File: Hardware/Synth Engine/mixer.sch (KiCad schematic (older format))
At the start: 62 parts, among them J2 Audio-Jack-2_Switch, U3 TL074, U8 PT2399

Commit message: add delay connector to main board and route it.
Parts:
- removed RV13: 20kA, Potentiometers:Potentiometer_Bourns_PTV09A-1_Horizontal, symbol POT
- removed RV14: 20k, Potentiometers:Potentiometer_Bourns_PTV09A-1_Horizontal, symbol POT
- removed RV15, RV16: 50kA, Potentiometers:Potentiometer_Bourns_PTV09A-1_Horizontal, symbol POT
- added J12: Conn_01x06, Pin_Headers:Pin_Header_Straight_1x06_Pitch2.54mm, symbol Conn_01x06
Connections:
- net labels added: delay_fb_ctrl_in, delay_fb_ctrl_out, delay_time_in, delay_time_out
- wire segments 140 -> 132
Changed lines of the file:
@@
 	0    1    1    0
-$EndComp
-$Comp
-L POT RV13
-U 1 1 5C54BC7D
-P 3650 2800
-F 0 "RV13" V 3475 2800 50  0000 C CNN
-F 1 "20kA" V 3550 2800 50  0000 C CNN
-F 2 "Potentiometers:Potentiometer_Bourns_PTV09A-1_Horizontal" H 3650 2800 50  0001 C CNN
-F 3 "" H 3650 2800 50  0001 C CNN
-	1    3650 2800
-	0    1    1    0
-$EndComp
-$Comp
-L GND #PWR072
-U 1 1 5C54BEBB
-P 3300 2850
-F 0 "#PWR072" H 3300 2600 50  0001 C CNN
-F 1 "GND" H 3300 2700 50  0000 C CNN
-F 2 "" H 3300 2850 50  0001 C CNN
-F 3 "" H 3300 2850 50  0001 C CNN
-	1    3300 2850
-	1    0    0    -1
 $EndComp
 Text Notes 2400 3050 0    60   ~ 0
@@
 $EndComp
 $Comp
-L GND #PWR073
+L GND #PWR072
 U 1 1 5C54C375
 P 4000 3250
-F 0 "#PWR073" H 4000 3000 50  0001 C CNN
+F 0 "#PWR072" H 4000 3000 50  0001 C CNN
 F 1 "GND" H 4000 3100 50  0000 C CNN
 F 2 "" H 4000 3250 50  0001 C CNN
@@
 $EndComp
 $Comp
-L GND #PWR074
+L GND #PWR073
 U 1 1 5C54C409
 P 4250 3400
-F 0 "#PWR074" H 4250 3150 50  0001 C CNN
+F 0 "#PWR073" H 4250 3150 50  0001 C CNN
 F 1 "GND" H 4250 3250 50  0000 C CNN
 F 2 "" H 4250 3400 50  0001 C CNN
@@
 $EndComp
 $Comp
-L GND #PWR075
+L GND #PWR074
 U 1 1 5C54D840
 P 6400 2650
-F 0 "#PWR075" H 6400 2400 50  0001 C CNN
+F 0 "#PWR074" H 6400 2400 50  0001 C CNN
 F 1 "GND" H 6400 2500 50  0000 C CNN
 F 2 "" H 6400 2650 50  0001 C CNN
@@
 $EndComp
 $Comp
-L GND #PWR076
+L GND #PWR075
 U 1 1 5C54DB09
 P 6850 2500
-F 0 "#PWR076" H 6850 2250 50  0001 C CNN
+F 0 "#PWR075" H 6850 2250 50  0001 C CNN
 F 1 "GND" H 6850 2350 50  0000 C CNN
 F 2 "" H 6850 2500 50  0001 C CNN
@@
 $EndComp
 $Comp
-L POT RV15
-U 1 1 5C54DE3E
-P 7400 2450
-F 0 "RV15" V 7225 2450 50  0000 C CNN
-F 1 "50kA" V 7300 2450 50  0000 C CNN
-F 2 "Potentiometers:Potentiometer_Bourns_PTV09A-1_Horizontal" H 7400 2450 50  0001 C CNN
-F 3 "" H 7400 2450 50  0001 C CNN
-	1    7400 2450
-	1    0    0    -1
-$EndComp
-$Comp
-L GND #PWR077
-U 1 1 5C54DF89
-P 7400 2600
-F 0 "#PWR077" H 7400 2350 50  0001 C CNN
-F 1 "GND" H 7400 2450 50  0000 C CNN
-F 2 "" H 7400 2600 50  0001 C CNN
-F 3 "" H 7400 2600 50  0001 C CNN
-	1    7400 2600
-	1    0    0    -1
-$EndComp
-$Comp
 L R R73
 U 1 1 5C54E024
@@
 	4200 2800 4350 2800
 Wire Wire Line
-	3300 2850 3300 2800
-Wire Wire Line
-	3300 2800 3500 2800
-Wire Wire Line
 	3650 2950 3850 2950
-Wire Wire Line
-	3850 2950 3850 2800
-Connection ~ 3850 2800
 Wire Wire Line
 	4250 3200 4250 3100
@@
 Connection ~ 6850 2250
 Wire Wire Line
-	7400 2300 7400 2250
-Wire Wire Line
-	7400 2250 7250 2250
+	7250 2250 7400 2250
 Wire Wire Line
 	5350 2200 5700 2200
@@
 $EndComp
 $Comp
-L GND #PWR078
+L GND #PWR076
 U 1 1 5C54F6A3
 P 5600 1450
-F 0 "#PWR078" H 5600 1200 50  0001 C CNN
+F 0 "#PWR076" H 5600 1200 50  0001 C CNN
 F 1 "GND" H 5600 1300 50  0000 C CNN
 F 2 "" H 5600 1450 50  0001 C CNN
@@
 $EndComp
 $Comp
-L GND #PWR079
+L GND #PWR077
 U 1 1 5C54FA05
 P 7150 1800
-F 0 "#PWR079" H 7150 1550 50  0001 C CNN
+F 0 "#PWR077" H 7150 1550 50  0001 C CNN
 F 1 "GND" H 7150 1650 50  0000 C CNN
 F 2 "" H 7150 1800 50  0001 C CNN
@@
 Text Label 4450 4400 0    60   ~ 0
 delay_in
-Text Label 9400 2350 0    60   ~ 0
+Text Label 9250 2100 0    60   ~ 0
 delay_out
 Wire Wire Line
-	9150 2100 9000 2100
+	9000 2100 9250 2100
 $Comp
 L R R74
@@
 $EndComp
 $Comp
-L GND #PWR080
+L GND #PWR078
 U 1 1 5C55157C
 P 8900 4800
-F 0 "#PWR080" H 8900 4550 50  0001 C CNN
+F 0 "#PWR078" H 8900 4550 50  0001 C CNN
 F 1 "GND" H 8900 4650 50  0000 C CNN
 F 2 "" H 8900 4800 50  0001 C CNN
@@
 $EndComp
 $Comp
-L +15V #PWR081
+L +15V #PWR079
 U 1 1 5C551582
 P 8900 4200
-F 0 "#PWR081" H 8900 4050 50  0001 C CNN
+F 0 "#PWR079" H 8900 4050 50  0001 C CNN
 F 1 "+15V" H 8900 4340 50  0000 C CNN
 F 2 "" H 8900 4200 50  0001 C CNN
@@
 	8450 4750 8450 4600
 $Comp
-L POT RV16
-U 1 1 5C5521F6
-P 9150 2350
-F 0 "RV16" V 8975 2350 50  0000 C CNN
-F 1 "50kA" V 9050 2350 50  0000 C CNN
-F 2 "Potentiometers:Potentiometer_Bourns_PTV09A-1_Horizontal" H 9150 2350 50  0001 C CNN
-F 3 "" H 9150 2350 50  0001 C CNN
-	1    9150 2350
-	1    0    0    -1
-$EndComp
-Wire Wire Line
-	9400 2350 9300 2350
-Wire Wire Line
-	9150 2200 9150 2100
-$Comp
-L GND #PWR082
-U 1 1 5C552581
-P 9150 2500
-F 0 "#PWR082" H 9150 2250 50  0001 C CNN
-F 1 "GND" H 9150 2350 50  0000 C CNN
-F 2 "" H 9150 2500 50  0001 C CNN
-F 3 "" H 9150 2500 50  0001 C CNN
-	1    9150 2500
-	1    0    0    -1
-$EndComp
-$Comp
 L R R59
 U 1 1 5C5902E2
@@
 $EndComp
 $Comp
-L GND #PWR083
+L GND #PWR080
 U 1 1 5C5902F7
 P 6400 4150
-F 0 "#PWR083" H 6400 3900 50  0001 C CNN
+F 0 "#PWR080" H 6400 3900 50  0001 C CNN
 F 1 "GND" H 6400 4000 50  0000 C CNN
 F 2 "" H 6400 4150 50  0001 C CNN
@@
 $EndComp
 $Comp
-L +15V #PWR084
+L +15V #PWR081
 U 1 1 5C5902FD
 P 6400 3550
-F 0 "#PWR084" H 6400 3400 50  0001 C CNN
+F 0 "#PWR081" H 6400 3400 50  0001 C CNN
 F 1 "+15V" H 6400 3690 50  0000 C CNN
 F 2 "" H 6400 3550 50  0001 C CNN
@@
 $EndComp
 $Comp
-L GND #PWR085
+L GND #PWR082
 U 1 1 5C59059B
 P 6400 5700
-F 0 "#PWR085" H 6400 5450 50  0001 C CNN
+F 0 "#PWR082" H 6400 5450 50  0001 C CNN
 F 1 "GND" H 6400 5550 50  0000 C CNN
 F 2 "" H 6400 5700 50  0001 C CNN
@@
 $EndComp
 $Comp
-L +15V #PWR086
+L +15V #PWR083
 U 1 1 5C5905A1
 P 6400 5100
-F 0 "#PWR086" H 6400 4950 50  0001 C CNN
+F 0 "#PWR083" H 6400 4950 50  0001 C CNN
 F 1 "+15V" H 6400 5240 50  0000 C CNN
 F 2 "" H 6400 5100 50  0001 C CNN
@@
 Text Label 4900 5500 0    60   ~ 0
 delay_out
-$Comp
-L POT RV14
-U 1 1 5C5914EB
-P 5150 4700
-F 0 "RV14" V 4975 4700 50  0000 C CNN
-F 1 "20k" V 5050 4700 50  0000 C CNN
-F 2 "Potentiometers:Potentiometer_Bourns_PTV09A-1_Horizontal" H 5150 4700 50  0001 C CNN
-F 3 "" H 5150 4700 50  0001 C CNN
-	1    5150 4700
-	1    0    0    -1
-$EndComp
 Wire Wire Line
 	5150 4550 5150 3950
@@
 	5150 4850 5150 5500
 Connection ~ 5150 5500
-$Comp
-L GND #PWR087
-U 1 1 5C5917F8
-P 5400 4750
-F 0 "#PWR087" H 5400 4500 50  0001 C CNN
-F 1 "GND" H 5400 4600 50  0000 C CNN
-F 2 "" H 5400 4750 50  0001 C CNN
-F 3 "" H 5400 4750 50  0001 C CNN
-	1    5400 4750
-	1    0    0    -1
-$EndComp
-Wire Wire Line
-	5400 4750 5400 4700
-Wire Wire Line
-	5400 4700 5300 4700
 Wire Wire Line
 	7350 3850 7350 4600
 Wire Wire Line
 	7350 5400 7350 4750
+$Comp
+L Conn_01x06 J12
+U 1 1 5C651FB4
+P 9550 2900
+F 0 "J12" H 9550 3200 50  0000 C CNN
+F 1 "Conn_01x06" H 9550 2500 50  0000 C CNN
+F 2 "Pin_Headers:Pin_Header_Straight_1x06_Pitch2.54mm" H 9550 2900 50  0001 C CNN
+F 3 "" H 9550 2900 50  0001 C CNN
+	1    9550 2900
+	1    0    0    -1
+$EndComp
+Text Label 7400 2250 0    60   ~ 0
+delay_fb_ctrl_in
+Text Label 7550 2450 2    60   ~ 0
+delay_fb_ctrl_out
+Text Label 9350 2700 2    60   ~ 0
+delay_fb_ctrl_in
+Text Label 9350 2800 2    60   ~ 0
+delay_fb_ctrl_out
+Text Label 3800 2800 2    60   ~ 0
+delay_time_in
+Text Label 3650 2950 2    60   ~ 0
+delay_time_out
+Text Label 9350 2900 2    60   ~ 0
+delay_time_in
+Text Label 9350 3000 2    60   ~ 0
+delay_time_out
+Text Label 9350 3100 2    60   ~ 0
+delay_in
+Text Label 9350 3200 2    60   ~ 0
+delay_out
+$Comp
+L GND #PWR084
+U 1 1 5C652A53
+P 3850 2950
+F 0 "#PWR084" H 3850 2700 50  0001 C CNN
+F 1 "GND" H 3850 2800 50  0000 C CNN
+F 2 "" H 3850 2950 50  0001 C CNN
+F 3 "" H 3850 2950 50  0001 C CNN
+	1    3850 2950
+	1    0    0    -1
+$EndComp
 $EndSCHEMATC

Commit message: fix remaining connector placement. Routing still WIP
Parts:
- removed J12: Conn_01x06, Pin_Headers:Pin_Header_Straight_1x06_Pitch2.54mm, symbol Conn_01x06
- added J5: Conn_01x08, Pin_Headers:Pin_Header_Straight_1x08_Pitch2.54mm, symbol Conn_01x08
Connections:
- net labels added: lfo_freq_in, lfo_freq_out
- wire segments 132 -> 134
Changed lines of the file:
@@
 Wire Wire Line
 	7350 5400 7350 4750
-$Comp
-L Conn_01x06 J12
-U 1 1 5C651FB4
-P 9550 2900
-F 0 "J12" H 9550 3200 50  0000 C CNN
-F 1 "Conn_01x06" H 9550 2500 50  0000 C CNN
-F 2 "Pin_Headers:Pin_Header_Straight_1x06_Pitch2.54mm" H 9550 2900 50  0001 C CNN
-F 3 "" H 9550 2900 50  0001 C CNN
-	1    9550 2900
-	1    0    0    -1
-$EndComp
 Text Label 7400 2250 0    60   ~ 0
 delay_fb_ctrl_in
@@
 	1    0    0    -1
 $EndComp
+Wire Wire Line
+	9000 3300 9350 3300
+Wire Wire Line
+	9000 3400 9350 3400
+Text HLabel 9000 3300 0    60   Output ~ 0
+lfo_freq_in
+Text HLabel 9000 3400 0    60   Input ~ 0
+lfo_freq_out
+$Comp
+L Conn_01x08 J5
+U 1 1 5C702327
+P 9550 3000
+F 0 "J5" H 9550 3400 50  0000 C CNN
+F 1 "Conn_01x08" H 9550 2500 50  0000 C CNN
+F 2 "Pin_Headers:Pin_Header_Straight_1x08_Pitch2.54mm" H 9550 3000 50  0001 C CNN
+F 3 "" H 9550 3000 50  0001 C CNN
+	1    9550 3000
+	1    0    0    -1
+$EndComp

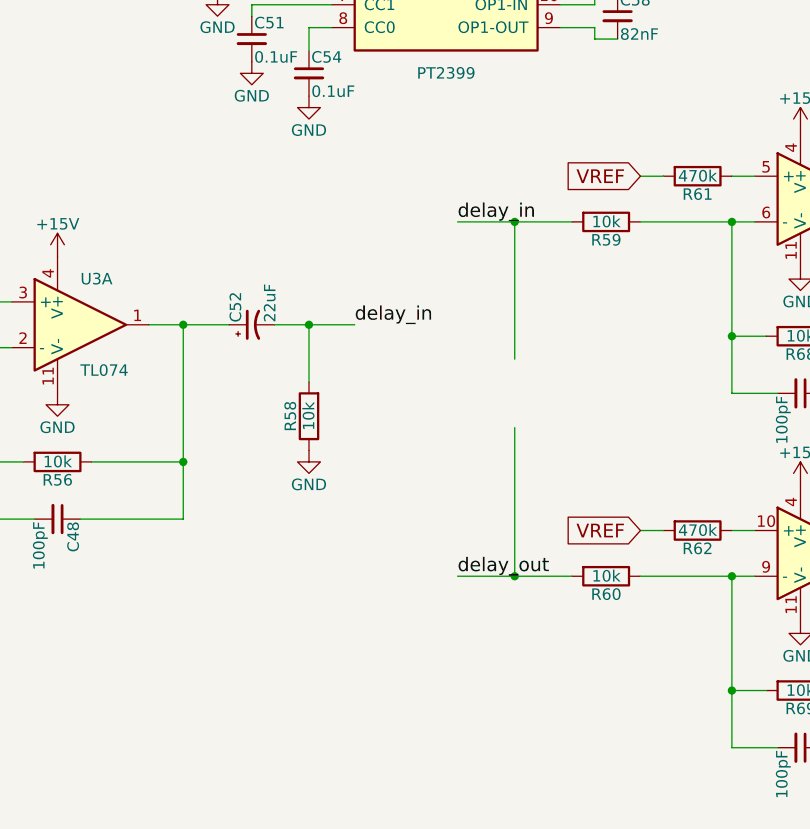
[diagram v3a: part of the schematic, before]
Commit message: redo connector routing with 2-row connectors
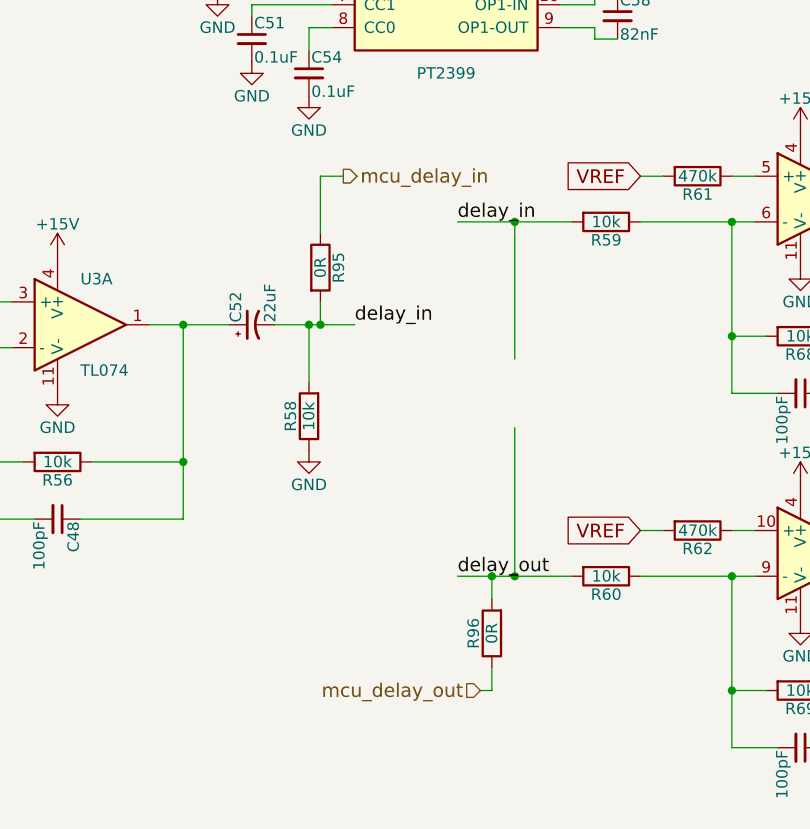
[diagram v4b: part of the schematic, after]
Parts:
- added R95, R96: 0R, digikey-footprints:0805, symbol R
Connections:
- net delay_in: now also R95.2
- net delay_out: now also R96.2
- new net mcu_delay_in: R95.1
- new net mcu_delay_out: R96.1
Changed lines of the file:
@@
 $EndComp
 $Comp
-L GND #PWR061
+L GND #PWR84
 U 1 1 5C394C8E
 P 10800 4700
-F 0 "#PWR061" H 10800 4450 50  0001 C CNN
+F 0 "#PWR84" H 10800 4450 50  0001 C CNN
 F 1 "GND" H 10800 4550 50  0000 C CNN
 F 2 "" H 10800 4700 50  0001 C CNN
@@
 $EndComp
 $Comp
-L GND #PWR062
+L GND #PWR62
 U 1 1 5C396479
 P 3150 4700
-F 0 "#PWR062" H 3150 4450 50  0001 C CNN
+F 0 "#PWR62" H 3150 4450 50  0001 C CNN
 F 1 "GND" H 3150 4550 50  0000 C CNN
 F 2 "" H 3150 4700 50  0001 C CNN
@@
 $EndComp
 $Comp
-L GND #PWR063
+L GND #PWR83
 U 1 1 5C39665C
 P 10200 5050
-F 0 "#PWR063" H 10200 4800 50  0001 C CNN
+F 0 "#PWR83" H 10200 4800 50  0001 C CNN
 F 1 "GND" H 10200 4900 50  0000 C CNN
 F 2 "" H 10200 5050 50  0001 C CNN
@@
 $EndComp
 $Comp
-L +15V #PWR064
+L +15V #PWR61
 U 1 1 5C396690
 P 3150 4100
-F 0 "#PWR064" H 3150 3950 50  0001 C CNN
+F 0 "#PWR61" H 3150 3950 50  0001 C CNN
 F 1 "+15V" H 3150 4240 50  0000 C CNN
 F 2 "" H 3150 4100 50  0001 C CNN
@@
 $EndComp
 $Comp
-L GND #PWR065
+L GND #PWR70
 U 1 1 5C55ADAC
 P 4250 4950
-F 0 "#PWR065" H 4250 4700 50  0001 C CNN
+F 0 "#PWR70" H 4250 4700 50  0001 C CNN
 F 1 "GND" H 4250 4800 50  0000 C CNN
 F 2 "" H 4250 4950 50  0001 C CNN
@@
 $EndComp
 $Comp
-L +5V #PWR066
+L +5V #PWR68
 U 1 1 5C54B4C5
 P 4100 1900
-F 0 "#PWR066" H 4100 1750 50  0001 C CNN
+F 0 "#PWR68" H 4100 1750 50  0001 C CNN
 F 1 "+5V" H 4100 2040 50  0000 C CNN
 F 2 "" H 4100 1900 50  0001 C CNN
@@
 $EndComp
 $Comp
-L GND #PWR067
+L GND #PWR63
 U 1 1 5C54B862
 P 3250 2350
-F 0 "#PWR067" H 3250 2100 50  0001 C CNN
+F 0 "#PWR63" H 3250 2100 50  0001 C CNN
 F 1 "GND" H 3250 2200 50  0000 C CNN
 F 2 "" H 3250 2350 50  0001 C CNN
@@
 $EndComp
 $Comp
-L GND #PWR068
+L GND #PWR64
 U 1 1 5C54B8B0
 P 3600 2350
-F 0 "#PWR068" H 3600 2100 50  0001 C CNN
+F 0 "#PWR64" H 3600 2100 50  0001 C CNN
 F 1 "GND" H 3600 2200 50  0000 C CNN
 F 2 "" H 3600 2350 50  0001 C CNN
@@
 $EndComp
 $Comp
-L GND #PWR069
+L GND #PWR71
 U 1 1 5C54B8F7
 P 4350 2400
-F 0 "#PWR069" H 4350 2150 50  0001 C CNN
+F 0 "#PWR71" H 4350 2150 50  0001 C CNN
 F 1 "GND" H 4350 2250 50  0000 C CNN
 F 2 "" H 4350 2400 50  0001 C CNN
@@
 $EndComp
 $Comp
-L GND #PWR070
+L GND #PWR67
 U 1 1 5C54B9BF
 P 4050 2450
-F 0 "#PWR070" H 4050 2200 50  0001 C CNN
+F 0 "#PWR67" H 4050 2200 50  0001 C CNN
 F 1 "GND" H 4050 2300 50  0000 C CNN
 F 2 "" H 4050 2450 50  0001 C CNN
@@
 $EndComp
 $Comp
-L GND #PWR071
+L GND #PWR72
 U 1 1 5C54BB6A
 P 4350 2500
-F 0 "#PWR071" H 4350 2250 50  0001 C CNN
+F 0 "#PWR72" H 4350 2250 50  0001 C CNN
 F 1 "GND" H 4350 2350 50  0000 C CNN
 F 2 "" H 4350 2500 50  0001 C CNN
@@
 $EndComp
 $Comp
-L GND #PWR072
+L GND #PWR66
 U 1 1 5C54C375
 P 4000 3250
-F 0 "#PWR072" H 4000 3000 50  0001 C CNN
+F 0 "#PWR66" H 4000 3000 50  0001 C CNN
 F 1 "GND" H 4000 3100 50  0000 C CNN
 F 2 "" H 4000 3250 50  0001 C CNN
@@
 $EndComp
 $Comp
-L GND #PWR073
+L GND #PWR69
 U 1 1 5C54C409
 P 4250 3400
-F 0 "#PWR073" H 4250 3150 50  0001 C CNN
+F 0 "#PWR69" H 4250 3150 50  0001 C CNN
 F 1 "GND" H 4250 3250 50  0000 C CNN
 F 2 "" H 4250 3400 50  0001 C CNN
@@
 $EndComp
 $Comp
-L GND #PWR074
+L GND #PWR74
 U 1 1 5C54D840
 P 6400 2650
-F 0 "#PWR074" H 6400 2400 50  0001 C CNN
+F 0 "#PWR74" H 6400 2400 50  0001 C CNN
 F 1 "GND" H 6400 2500 50  0000 C CNN
 F 2 "" H 6400 2650 50  0001 C CNN
@@
 $EndComp
 $Comp
-L GND #PWR075
+L GND #PWR79
 U 1 1 5C54DB09
 P 6850 2500
-F 0 "#PWR075" H 6850 2250 50  0001 C CNN
+F 0 "#PWR79" H 6850 2250 50  0001 C CNN
 F 1 "GND" H 6850 2350 50  0000 C CNN
 F 2 "" H 6850 2500 50  0001 C CNN
@@
 $EndComp
 $Comp
-L GND #PWR076
+L GND #PWR73
 U 1 1 5C54F6A3
 P 5600 1450
-F 0 "#PWR076" H 5600 1200 50  0001 C CNN
+F 0 "#PWR73" H 5600 1200 50  0001 C CNN
 F 1 "GND" H 5600 1300 50  0000 C CNN
 F 2 "" H 5600 1450 50  0001 C CNN
@@
 $EndComp
 $Comp
-L GND #PWR077
+L GND #PWR80
 U 1 1 5C54FA05
 P 7150 1800
-F 0 "#PWR077" H 7150 1550 50  0001 C CNN
+F 0 "#PWR80" H 7150 1550 50  0001 C CNN
 F 1 "GND" H 7150 1650 50  0000 C CNN
 F 2 "" H 7150 1800 50  0001 C CNN
@@
 $EndComp
 $Comp
-L GND #PWR078
+L GND #PWR82
 U 1 1 5C55157C
 P 8900 4800
-F 0 "#PWR078" H 8900 4550 50  0001 C CNN
+F 0 "#PWR82" H 8900 4550 50  0001 C CNN
 F 1 "GND" H 8900 4650 50  0000 C CNN
 F 2 "" H 8900 4800 50  0001 C CNN
@@
 $EndComp
 $Comp
-L +15V #PWR079
+L +15V #PWR81
 U 1 1 5C551582
 P 8900 4200
-F 0 "#PWR079" H 8900 4050 50  0001 C CNN
+F 0 "#PWR81" H 8900 4050 50  0001 C CNN
 F 1 "+15V" H 8900 4340 50  0000 C CNN
 F 2 "" H 8900 4200 50  0001 C CNN
@@
 $EndComp
 $Comp
-L GND #PWR080
+L GND #PWR76
 U 1 1 5C5902F7
 P 6400 4150
-F 0 "#PWR080" H 6400 3900 50  0001 C CNN
+F 0 "#PWR76" H 6400 3900 50  0001 C CNN
 F 1 "GND" H 6400 4000 50  0000 C CNN
 F 2 "" H 6400 4150 50  0001 C CNN
@@
 $EndComp
 $Comp
-L +15V #PWR081
+L +15V #PWR75
 U 1 1 5C5902FD
 P 6400 3550
-F 0 "#PWR081" H 6400 3400 50  0001 C CNN
+F 0 "#PWR75" H 6400 3400 50  0001 C CNN
 F 1 "+15V" H 6400 3690 50  0000 C CNN
 F 2 "" H 6400 3550 50  0001 C CNN
@@
 $EndComp
 $Comp
-L GND #PWR082
+L GND #PWR78
 U 1 1 5C59059B
 P 6400 5700
-F 0 "#PWR082" H 6400 5450 50  0001 C CNN
+F 0 "#PWR78" H 6400 5450 50  0001 C CNN
 F 1 "GND" H 6400 5550 50  0000 C CNN
 F 2 "" H 6400 5700 50  0001 C CNN
@@
 $EndComp
 $Comp
-L +15V #PWR083
+L +15V #PWR77
 U 1 1 5C5905A1
 P 6400 5100
-F 0 "#PWR083" H 6400 4950 50  0001 C CNN
+F 0 "#PWR77" H 6400 4950 50  0001 C CNN
 F 1 "+15V" H 6400 5240 50  0000 C CNN
 F 2 "" H 6400 5100 50  0001 C CNN
@@
 delay_out
 $Comp
-L GND #PWR084
+L GND #PWR65
 U 1 1 5C652A53
 P 3850 2950
-F 0 "#PWR084" H 3850 2700 50  0001 C CNN
+F 0 "#PWR65" H 3850 2700 50  0001 C CNN
 F 1 "GND" H 3850 2800 50  0000 C CNN
 F 2 "" H 3850 2950 50  0001 C CNN
@@
 	1    0    0    -1
 $EndComp
+$Comp
+L R R95
+U 1 1 5C709E3D
+P 4300 4150
+F 0 "R95" V 4380 4150 50  0000 C CNN
+F 1 "0R" V 4300 4150 50  0000 C CNN
+F 2 "digikey-footprints:0805" V 4230 4150 50  0001 C CNN
+F 3 "" H 4300 4150 50  0001 C CNN
+	1    4300 4150
+	1    0    0    -1
+$EndComp
+Wire Wire Line
+	4300 4300 4300 4400
+Connection ~ 4300 4400
+$Comp
+L R R96
+U 1 1 5C70A143
+P 5050 5750
+F 0 "R96" V 5130 5750 50  0000 C CNN
+F 1 "0R" V 5050 5750 50  0000 C CNN
+F 2 "digikey-footprints:0805" V 4980 5750 50  0001 C CNN
+F 3 "" H 5050 5750 50  0001 C CNN
+	1    5050 5750
+	-1   0    0    1
+$EndComp
+Wire Wire Line
+	5050 5600 5050 5500
+Connection ~ 5050 5500
+Text HLabel 4400 3750 2    60   Output ~ 0
+mcu_delay_in
+Text HLabel 5000 6000 0    60   Input ~ 0
+mcu_delay_out
+Wire Wire Line
+	4300 4000 4300 3750
+Wire Wire Line
+	4300 3750 4400 3750
+Wire Wire Line
+	5000 6000 5050 6000
+Wire Wire Line
+	5050 6000 5050 5900
 $EndSCHEMATC

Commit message: new release candidate. Passes DRC.
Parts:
- J2: footprint Connectors:PINHEAD1-3 -> Connectors_Molex:Molex_KK-6410-03_03x2.54mm_Straight
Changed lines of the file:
@@
 F 0 "J2" H 10550 4775 50  0000 C CNN
 F 1 "Audio-Jack-2_Switch" H 10825 4525 50  0000 C CNN
-F 2 "Connectors:PINHEAD1-3" H 10850 4700 50  0001 C CNN
+F 2 "Connectors_Molex:Molex_KK-6410-03_03x2.54mm_Straight" H 10850 4700 50  0001 C CNN
 F 3 "" H 10850 4700 50  0001 C CNN
 	1    10600 4600

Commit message: arrange reference designators on main board
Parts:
- J2: footprint Connectors_Molex:Molex_KK-6410-03_03x2.54mm_Straight -> Pin_Headers:Pin_Header_Straight_1x03_Pitch2.00mm
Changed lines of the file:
@@
 F 0 "J2" H 10550 4775 50  0000 C CNN
 F 1 "Audio-Jack-2_Switch" H 10825 4525 50  0000 C CNN
-F 2 "Connectors_Molex:Molex_KK-6410-03_03x2.54mm_Straight" H 10850 4700 50  0001 C CNN
+F 2 "Pin_Headers:Pin_Header_Straight_1x03_Pitch2.00mm" H 10850 4700 50  0001 C CNN
 F 3 "" H 10850 4700 50  0001 C CNN
 	1    10600 4600
